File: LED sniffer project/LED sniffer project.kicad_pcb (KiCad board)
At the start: 2 copper layers, 85 x 58.5 mm, 13 parts, among them J1 Conn_01x02_Pin, Q1 2N3904, SW1 Push_Button

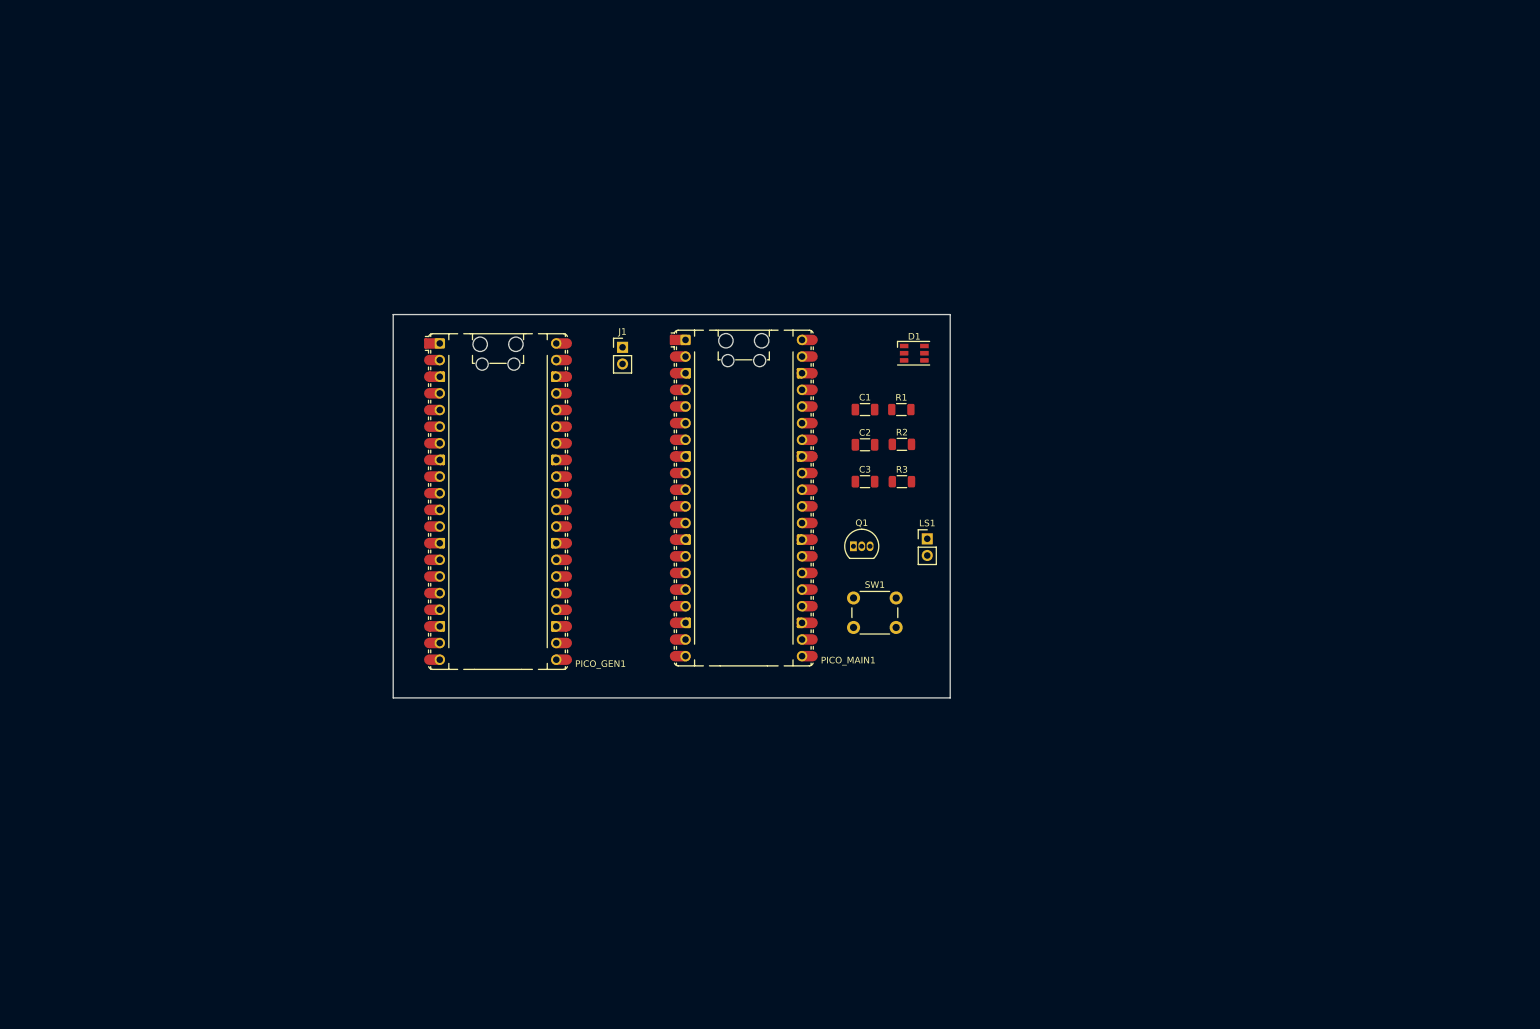
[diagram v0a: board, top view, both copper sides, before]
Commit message: aaron's PCB file for CAD rough draft (contains 2 raspberry pi)
I was thinking at some point that the jumper is not needed since imagine we could be connecting the raspberry pi with usb power....
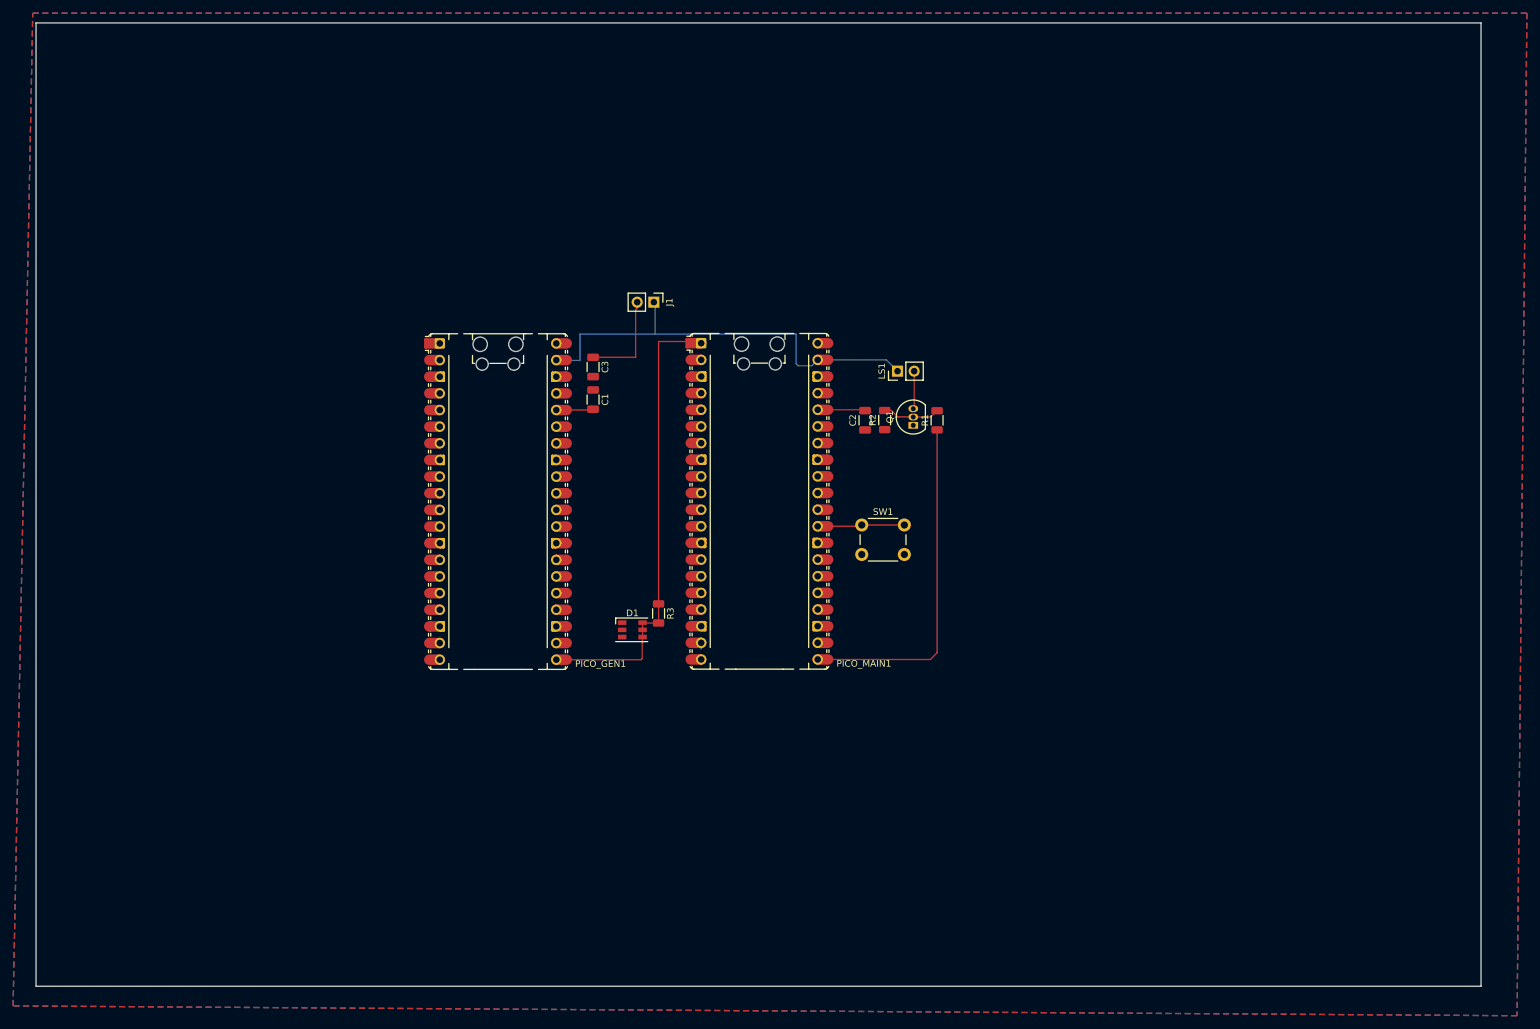
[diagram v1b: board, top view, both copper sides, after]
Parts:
- moved D1 60.3 mm to (134.5, 110.6)
- moved C3 45.0 mm to (128.5, 70.5), turned to -90 degrees
- moved R3 42.2 mm to (138.5, 108.1), turned to -90 degrees
- moved C1 41.5 mm to (128.5, 75.5), turned to -90 degrees
- moved LS1 26.0 mm to (175.0, 71.1), turned to 90 degrees
- moved Q1 20.6 mm to (177.4, 79.4), turned to 90 degrees
- moved SW1 11.2 mm to (169.5, 94.6)
- moved J1 8.38 mm to (137.8, 60.6), turned to -90 degrees
- moved R1 5.70 mm to (181.0, 78.6), turned to 90 degrees
- moved R2 4.55 mm to (173.0, 78.6), turned to 90 degrees
- moved C2 3.73 mm to (170.0, 78.6), turned to 90 degrees
- moved PICO_MAIN1 2.44 mm to (153.9, 91.0)
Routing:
- net /Din: track 0.00 -> 70.7 mm
- net 5V: track 0.00 -> 66.3 mm
- net /SPEAKER_OUT: track 0.00 -> 52.7 mm
- net Net-(J1-Pin_2): track 0.00 -> 15.0 mm
- net /BTN_IN: track 0.00 -> 13.3 mm
- net Net-(Q1-B): track 0.00 -> 8.81 mm
- net Net-(PICO_MAIN1-3V3): track 0.00 -> 7.27 mm
- net Net-(Q1-C): track 0.00 -> 5.79 mm
- net Net-(PICO_GEN1-3V3): track 0.00 -> 5.66 mm
- net unconnected-(PICO_MAIN1-GPIO14-Pad19): track 0.00 -> 0.92 mm
- added copper zone on B.Cu, net GND
- added copper zone on F.Cu, net GND
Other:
- board size 85 x 58.5 mm -> 220.5 x 147 mm

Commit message: rough draft of schematic
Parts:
- removed C1, C2: 0.1u, Capacitor_SMD:C_1206_3216Metric
- removed C3: 50u, Capacitor_SMD:C_1206_3216Metric
- removed D1: LED_RGB, LED_SMD:LED_RGB_PLCC-6
- removed LS1: Speaker, Connector_PinHeader_2.54mm:PinHeader_1x02_P2.54mm_Vertical
- removed PICO_GEN1: RaspberryPi_Pico, Module:RaspberryPi_Pico_Common_Unspecified
- removed Q1: 2N3904, Package_TO_SOT_THT:TO-92_Inline
- removed R1: 1k, Resistor_SMD:R_1206_3216Metric
- removed R2: 100k, Resistor_SMD:R_1206_3216Metric
- removed R3: 330, Resistor_SMD:R_1206_3216Metric
- added J2: Conn_01x03, Connector_PinHeader_1.00mm:PinHeader_1x03_P1.00mm_Vertical, F.Cu at (151.0, 52.5)
- J1: value Conn_01x02_Pin -> Conn_01x02; footprint Connector_PinHeader_2.54mm:PinHeader_1x02_P2.54mm_Vertical -> Connector_PinHeader_1.00mm:PinHeader_1x02_P1.00mm_Vertical
- moved J1 43.8 mm to (150.5, 102.5), turned to 90 degrees
- moved SW1 23.5 mm to (150.3, 81.0)
- moved PICO_MAIN1 21.8 mm to (137.1, 77.1)
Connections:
- J1 pad 1: 5V -> Net-(J1-Pin_1)
- J1 pad 2: Net-(J1-Pin_2) -> GND
- PICO_MAIN1 pad 1: /Din -> unconnected-(PICO_MAIN1-GPIO0-Pad1)
- PICO_MAIN1 pad 21: /SPEAKER_OUT -> Net-(J1-Pin_1)
- PICO_MAIN1 pad 36: Net-(PICO_MAIN1-3V3) -> unconnected-(PICO_MAIN1-3V3-Pad36)
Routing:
- net /Din: track 70.7 -> 0.00 mm
- net 5V: track 66.3 -> 7.75 mm
- net /SPEAKER_OUT: track 52.7 -> 0.00 mm
- net unconnected-(J2-Pin_2-Pad2): track 0.00 -> 19.0 mm
- net Net-(J1-Pin_2): track 15.0 -> 0.00 mm
- net GND: track 0.00 -> 10.8 mm
- net Net-(Q1-B): track 8.81 -> 0.00 mm
- net Net-(PICO_MAIN1-3V3): track 7.27 -> 0.00 mm
- net Net-(Q1-C): track 5.79 -> 0.00 mm
- net Net-(PICO_GEN1-3V3): track 5.66 -> 0.00 mm
- net Net-(J1-Pin_1): track 0.00 -> 4.24 mm
- net /BTN_IN: track 13.3 -> 10.0 mm
- net unconnected-(PICO_MAIN1-GPIO14-Pad19): track 0.92 -> 0.00 mm
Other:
- board outline removed

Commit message: Updated CAD
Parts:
- added D1: SK6812, LED_SMD:LED_SK6812_PLCC4_5.0x5.0mm_P3.2mm, F.Cu at (154.2, 67.8)
- added J3: Conn_01x03, Connector_PinHeader_2.54mm:PinHeader_1x03_P2.54mm_Vertical, F.Cu at (160.8, 99.3)
- added J4: Conn_01x04, Connector_PinHeader_2.54mm:PinHeader_1x04_P2.54mm_Vertical, F.Cu at (155.8, 99.3)
- added J5: Conn_01x04, Connector_PinHeader_2.54mm:PinHeader_1x04_P2.54mm_Vertical, F.Cu at (159.5, 55.4)
- added R1: 22k, Resistor_THT:R_Axial_DIN0207_L6.3mm_D2.5mm_P10.16mm_Horizontal, F.Cu at (165.8, 71.1)
- added R2: 33k, Resistor_THT:R_Axial_DIN0207_L6.3mm_D2.5mm_P10.16mm_Horizontal, F.Cu at (165.8, 84.6)
- J1: footprint Connector_PinHeader_1.00mm:PinHeader_1x02_P1.00mm_Vertical -> Connector_PinHeader_2.54mm:PinHeader_1x02_P2.54mm_Vertical
- J2: footprint Connector_PinHeader_1.00mm:PinHeader_1x03_P1.00mm_Vertical -> Connector_PinHeader_2.54mm:PinHeader_1x03_P2.54mm_Vertical
- moved J1 15.3 mm to (165.5, 99.3), turned to 180 degrees
- moved J2 4.61 mm to (154.5, 55.5), turned to 0 degrees
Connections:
- J2 pad 2: unconnected-(J2-Pin_2-Pad2) -> Net-(D1-DIN)
- PICO_MAIN1 pad 22: unconnected-(PICO_MAIN1-GPIO17-Pad22) -> Net-(J3-Pin_2)
- PICO_MAIN1 pad 24: unconnected-(PICO_MAIN1-GPIO18-Pad24) -> Net-(J4-Pin_3)
- PICO_MAIN1 pad 32: unconnected-(PICO_MAIN1-GPIO27_ADC1-Pad32) -> Net-(PICO_MAIN1-GPIO27_ADC1)
- PICO_MAIN1 pad 34: unconnected-(J2-Pin_2-Pad2) -> Net-(J5-Pin_3)
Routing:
- net Net-(J5-Pin_3): track 0.00 -> 30.5 mm
- net Net-(PICO_MAIN1-GPIO27_ADC1): track 0.00 -> 23.6 mm
- net Net-(D1-DIN): track 0.00 -> 20.7 mm
- net unconnected-(J2-Pin_2-Pad2): track 19.0 -> 0.00 mm
- net 5V: track 7.75 -> 23.5 mm
- net Net-(J1-Pin_1): track 4.24 -> 19.9 mm
- net Net-(J3-Pin_2): track 0.00 -> 14.8 mm
- net Net-(J4-Pin_3): track 0.00 -> 9.21 mm
- net unconnected-(PICO_MAIN1-3V3_EN-Pad37)_1: track 0.00 -> 1.71 mm
- net GND: vias 0 -> 65
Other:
- board outline added: 44 x 52.2 mm
- board text added: "Team 09"

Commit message: Slight update
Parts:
- added R3: 22k, Resistor_SMD:R_0603_1608Metric, F.Cu at (162.8, 67.2)
- added R4: 33k, Resistor_SMD:R_0603_1608Metric, F.Cu at (159.5, 67.2)
- R1, R2: footprint Resistor_THT:R_Axial_DIN0207_L6.3mm_D2.5mm_P10.16mm_Horizontal -> Resistor_SMD:R_0603_1608Metric
- moved R2 25.8 mm to (165.0, 58.8), turned to -90 degrees
- moved R1 12.6 mm to (163.0, 58.8)
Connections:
- PICO_MAIN1 pad 34: Net-(J5-Pin_3) -> Net-(PICO_MAIN1-GPIO28_ADC2)
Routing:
- net Net-(PICO_MAIN1-GPIO28_ADC2): track 0.00 -> 24.2 mm
- net Net-(J5-Pin_3): track 30.5 -> 7.26 mm
- net Net-(PICO_MAIN1-GPIO27_ADC1): track 23.6 -> 33.3 mm
- net Net-(D1-DIN): track 20.7 -> 16.6 mm
- net GND: vias 65 -> 76
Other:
- board text added: "Team 09 Nameless Nineski V1.0 2025.11.20"
- board text removed: "Team 09"

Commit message: Even more updated
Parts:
- moved R4 1.75 mm to (161.2, 67.2), turned to -90 degrees
- moved R2 0.50 mm to (164.5, 58.8)
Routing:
- net Net-(PICO_MAIN1-GPIO28_ADC2): track 24.2 -> 21.7 mm
- net Net-(PICO_MAIN1-GPIO27_ADC1): track 33.3 -> 32.8 mm
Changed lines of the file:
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@@
 	(footprint "Resistor_SMD:R_0603_1608Metric"
 		(layer "F.Cu")
-		(at 165 58.75 -90)
+		(at 164.5 58.75 -90)
 		(descr "Resistor SMD 0603 (1608 Metric), square (rectangular) end terminal, IPC-7351 nominal, (Body size source: IPC-SM-782 page 72, https://www.pcb-3d.com/wordpress/wp-content/uploads/ipc-sm-782a_amendment_1_and_2.pdf), generated with kicad-footprint-generator")
 		(tags "resistor")
@@
 		(tags "resistor")
 		(property "Reference" "R3"
-			(at 0 -1.43 90)
+			(at 0 1.5 90)
 			(layer "F.SilkS")
 			(effects
@@
 	(footprint "Resistor_SMD:R_0603_1608Metric"
 		(layer "F.Cu")
-		(at 159.5 67.25 90)
+		(at 161.25 67.25 -90)
 		(descr "Resistor SMD 0603 (1608 Metric), square (rectangular) end terminal, IPC-7351 nominal, (Body size source: IPC-SM-782 page 72, https://www.pcb-3d.com/wordpress/wp-content/uploads/ipc-sm-782a_amendment_1_and_2.pdf), generated with kicad-footprint-generator")
 		(tags "resistor")
 		(property "Reference" "R4"
-			(at 0 -1.43 90)
+			(at 0 1.25 90)
 			(layer "F.SilkS")
 			(effects
@@
 		(attr smd)
 		(fp_line
-			(start -0.237258 -0.5225)
-			(end 0.237258 -0.5225)
+			(start -0.237258 0.5225)
+			(end 0.237258 0.5225)
 			(stroke
 				(width 0.12)
@@
 		)
 		(fp_line
-			(start -0.237258 0.5225)
-			(end 0.237258 0.5225)
+			(start -0.237258 -0.5225)
+			(end 0.237258 -0.5225)
 			(stroke
 				(width 0.12)
@@
 		)
 		(fp_line
-			(start 1.48 -0.73)
-			(end 1.48 0.73)
+			(start -1.48 0.73)
+			(end -1.48 -0.73)
 			(stroke
 				(width 0.05)
@@
 		)
 		(fp_line
-			(start -1.48 -0.73)
-			(end 1.48 -0.73)
+			(start 1.48 0.73)
+			(end -1.48 0.73)
 			(stroke
 				(width 0.05)
@@
 		)
 		(fp_line
-			(start 1.48 0.73)
-			(end -1.48 0.73)
+			(start -1.48 -0.73)
+			(end 1.48 -0.73)
 			(stroke
 				(width 0.05)
@@
 		)
 		(fp_line
-			(start -1.48 0.73)
-			(end -1.48 -0.73)
+			(start 1.48 -0.73)
+			(end 1.48 0.73)
 			(stroke
 				(width 0.05)
@@
 		)
 		(fp_line
-			(start 0.8 -0.4125)
-			(end 0.8 0.4125)
+			(start -0.8 0.4125)
+			(end -0.8 -0.4125)
 			(stroke
 				(width 0.1)
@@
 		)
 		(fp_line
-			(start -0.8 -0.4125)
-			(end 0.8 -0.4125)
+			(start 0.8 0.4125)
+			(end -0.8 0.4125)
 			(stroke
 				(width 0.1)
@@
 		)
 		(fp_line
-			(start 0.8 0.4125)
-			(end -0.8 0.4125)
+			(start -0.8 -0.4125)
+			(end 0.8 -0.4125)
 			(stroke
 				(width 0.1)
@@
 		)
 		(fp_line
-			(start -0.8 0.4125)
-			(end -0.8 -0.4125)
+			(start 0.8 -0.4125)
+			(end 0.8 0.4125)
 			(stroke
 				(width 0.1)
@@
 		)
 		(pad "1" smd roundrect
-			(at -0.825 0 90)
+			(at -0.825 0 270)
 			(size 0.8 0.95)
 			(layers "F.Cu" "F.Mask" "F.Paste")
@@
 		)
 		(pad "2" smd roundrect
-			(at 0.825 0 90)
+			(at 0.825 0 270)
 			(size 0.8 0.95)
 			(layers "F.Cu" "F.Mask" "F.Paste")
@@
 	)
 	(gr_text "Team 09\nNameless Nineski\nV1.0\n2025.11.20"
-		(at 133.5 90.25 270)
-		(layer "B.SilkS")
+		(at 158.5 74.5 270)
+		(layer "F.SilkS")
 		(effects
 			(font
-				(size 1.5 1.5)
+				(size 1.4 1.4)
 				(thickness 0.3)
 				(bold yes)
 			)
-			(justify left bottom mirror)
+			(justify left bottom)
 		)
 	)
@@
 	)
 	(segment
-		(start 163 59.575)
-		(end 165 59.575)
+		(start 146.8 73.28)
+		(end 147.02 73.5)
 		(width 0.5)
 		(layer "F.Cu")
@@
 	)
 	(segment
-		(start 146.8 73.28)
-		(end 147.02 73.5)
+		(start 163 73.5)
+		(end 164.25 72.25)
 		(width 0.5)
 		(layer "F.Cu")
@@
 	)
 	(segment
-		(start 163 73.5)
-		(end 164.25 72.25)
+		(start 163 59.575)
+		(end 164.5 59.575)
 		(width 0.5)
 		(layer "F.Cu")
@@
 	)
 	(segment
+		(start 161.25 68.075)
+		(end 162.75 68.075)
+		(width 0.2)
+		(layer "F.Cu")
+		(net 63)
+	)
+	(segment
 		(start 162.75 69.25)
 		(end 160.5 71.5)
@@
 		(width 0.5)
 		(layer "F.Cu")
-		(net 63)
-	)
-	(segment
-		(start 162.75 68.075)
-		(end 161.15 68.075)
-		(width 0.5)
-		(layer "F.Cu")
-		(net 63)
-	)
-	(segment
-		(start 161.15 68.075)
-		(end 159.5 66.425)
-		(width 0.5)
-		(layer "F.Cu")

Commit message: Possible submission
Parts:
- added J6: Conn_01x04, Connector_PinHeader_2.54mm:PinHeader_1x04_P2.54mm_Vertical, F.Cu at (158.1, 104.2)
- J1: value Conn_01x02 -> Conn_01x03; footprint Connector_PinHeader_2.54mm:PinHeader_1x02_P2.54mm_Vertical -> Connector_PinHeader_2.54mm:PinHeader_1x03_P2.54mm_Vertical
- J2: value Conn_01x03 -> Conn_01x04; footprint Connector_PinHeader_2.54mm:PinHeader_1x03_P2.54mm_Vertical -> Connector_PinHeader_2.54mm:PinHeader_1x04_P2.54mm_Vertical
- J3: value Conn_01x03 -> Conn_01x02; footprint Connector_PinHeader_2.54mm:PinHeader_1x03_P2.54mm_Vertical -> Connector_PinHeader_2.54mm:PinHeader_1x02_P2.54mm_Vertical
- J4: value Conn_01x04 -> Conn_01x03; footprint Connector_PinHeader_2.54mm:PinHeader_1x04_P2.54mm_Vertical -> Connector_PinHeader_2.54mm:PinHeader_1x03_P2.54mm_Vertical
- moved J1 47.3 mm to (151.2, 54.2), turned to 0 degrees
- moved J5 38.9 mm to (152.0, 93.6), turned to 180 degrees
- moved R1 28.1 mm to (165.2, 86.8)
- moved R2 28.0 mm to (163.8, 86.8)
- moved R3 16.7 mm to (165.2, 83.8)
- moved R4 16.7 mm to (163.8, 83.8)
- moved D1 14.7 mm to (162.0, 55.2)
- moved SW1 13.6 mm to (155.0, 68.2)
- moved J4 5.86 mm to (156.8, 93.5)
- moved J3 5.79 mm to (161.2, 93.5)
- moved J2 1.65 mm to (155.5, 54.2)
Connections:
- J1 pad 1: Net-(J1-Pin_1) -> 5V
- J1 pad 2: GND -> Net-(D1-DIN)
- J2 pad 3: GND -> Net-(J2-Pin_3)
- J3 pad 1: Net-(J1-Pin_1) -> Net-(J3-Pin_1)
- J3 pad 2: Net-(J3-Pin_2) -> GND
- J4 pad 1: Net-(J1-Pin_1) -> Net-(J3-Pin_1)
- J4 pad 2: Net-(J3-Pin_2) -> Net-(J4-Pin_2)
- J4 pad 3: Net-(J4-Pin_3) -> GND
- J5 pad 1: 5V -> Net-(J3-Pin_1)
- J5 pad 2: Net-(D1-DIN) -> Net-(J4-Pin_2)
- PICO_MAIN1 pad 17: unconnected-(PICO_MAIN1-GPIO13-Pad17)_1 -> Net-(J6-Pin_4)
- PICO_MAIN1 pad 19: unconnected-(PICO_MAIN1-GPIO14-Pad19) -> Net-(J6-Pin_3)
- PICO_MAIN1 pad 20: unconnected-(PICO_MAIN1-GPIO15-Pad20) -> Net-(J6-Pin_2)
- PICO_MAIN1 pad 21: Net-(J1-Pin_1) -> Net-(PICO_MAIN1-GPIO16)
- PICO_MAIN1 pad 22: Net-(J3-Pin_2) -> Net-(PICO_MAIN1-GPIO17)
- PICO_MAIN1 pad 24: Net-(J4-Pin_3) -> Net-(J3-Pin_1)
- PICO_MAIN1 pad 25: unconnected-(PICO_MAIN1-GPIO19-Pad25) -> Net-(J4-Pin_2)
- PICO_MAIN1 pad 26: unconnected-(PICO_MAIN1-GPIO20-Pad26)_1 -> Net-(J5-Pin_3)
- PICO_MAIN1 pad 29: /BTN_IN -> unconnected-(PICO_MAIN1-GPIO22-Pad29)
- PICO_MAIN1 pad 32: Net-(PICO_MAIN1-GPIO27_ADC1) -> unconnected-(PICO_MAIN1-GPIO27_ADC1-Pad32)_1
- R1 pad 1: Net-(PICO_MAIN1-GPIO27_ADC1) -> Net-(PICO_MAIN1-GPIO16)
- R2 pad 2: Net-(PICO_MAIN1-GPIO27_ADC1) -> Net-(PICO_MAIN1-GPIO16)
- R3 pad 1: Net-(PICO_MAIN1-GPIO28_ADC2) -> Net-(PICO_MAIN1-GPIO17)
- R3 pad 2: Net-(J5-Pin_3) -> Net-(J2-Pin_3)
- R4 pad 2: Net-(PICO_MAIN1-GPIO28_ADC2) -> Net-(PICO_MAIN1-GPIO17)
- SW1 pad 1: /BTN_IN -> Net-(PICO_MAIN1-GPIO28_ADC2)
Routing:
- net Net-(PICO_MAIN1-GPIO17): track 0.00 -> 33.2 mm
- net Net-(D1-DIN): track 16.6 -> 49.7 mm
- net Net-(PICO_MAIN1-GPIO27_ADC1): track 32.8 -> 0.00 mm
- net Net-(PICO_MAIN1-GPIO16): track 0.00 -> 32.0 mm
- net Net-(J6-Pin_2): track 0.00 -> 30.6 mm
- net Net-(J6-Pin_3): track 0.00 -> 29.1 mm
- net Net-(J2-Pin_3): track 0.00 -> 28.4 mm
- net Net-(J6-Pin_4): track 0.00 -> 26.6 mm
- net Net-(J1-Pin_1): track 19.9 -> 0.00 mm
- net Net-(J3-Pin_1): track 0.00 -> 15.3 mm
- net Net-(J3-Pin_2): track 14.8 -> 0.00 mm
- net GND: track 10.8 -> 0.00 mm, vias 76 -> 106
- net Net-(J4-Pin_2): track 0.00 -> 10.8 mm
- net /BTN_IN: track 10.0 -> 0.00 mm
- net Net-(J4-Pin_3): track 9.21 -> 0.00 mm
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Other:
- board size 44 x 52.2 mm -> 43.8 x 59.2 mm
